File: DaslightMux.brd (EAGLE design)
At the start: 60 x 55.9 mm, 8 parts, among them U1 XC9572XL_TQ100

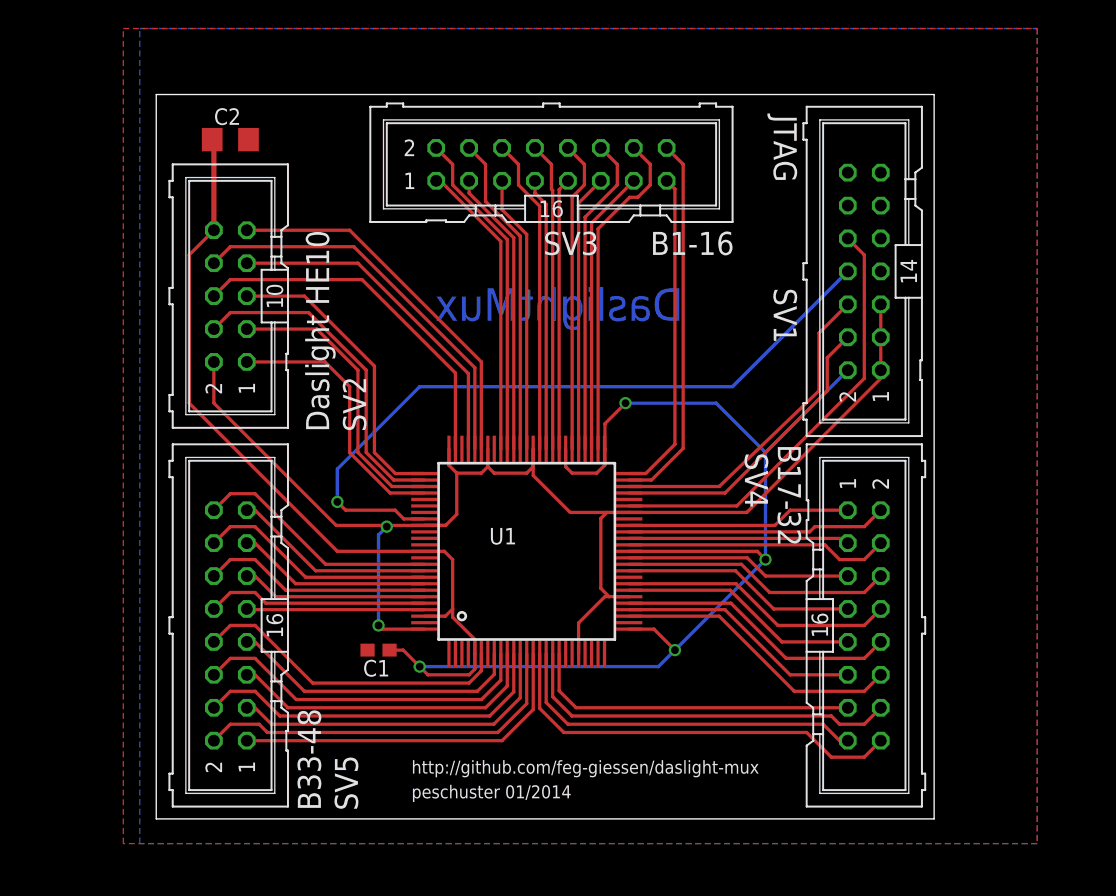
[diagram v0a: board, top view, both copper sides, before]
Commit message: Cleanup, enclosure.
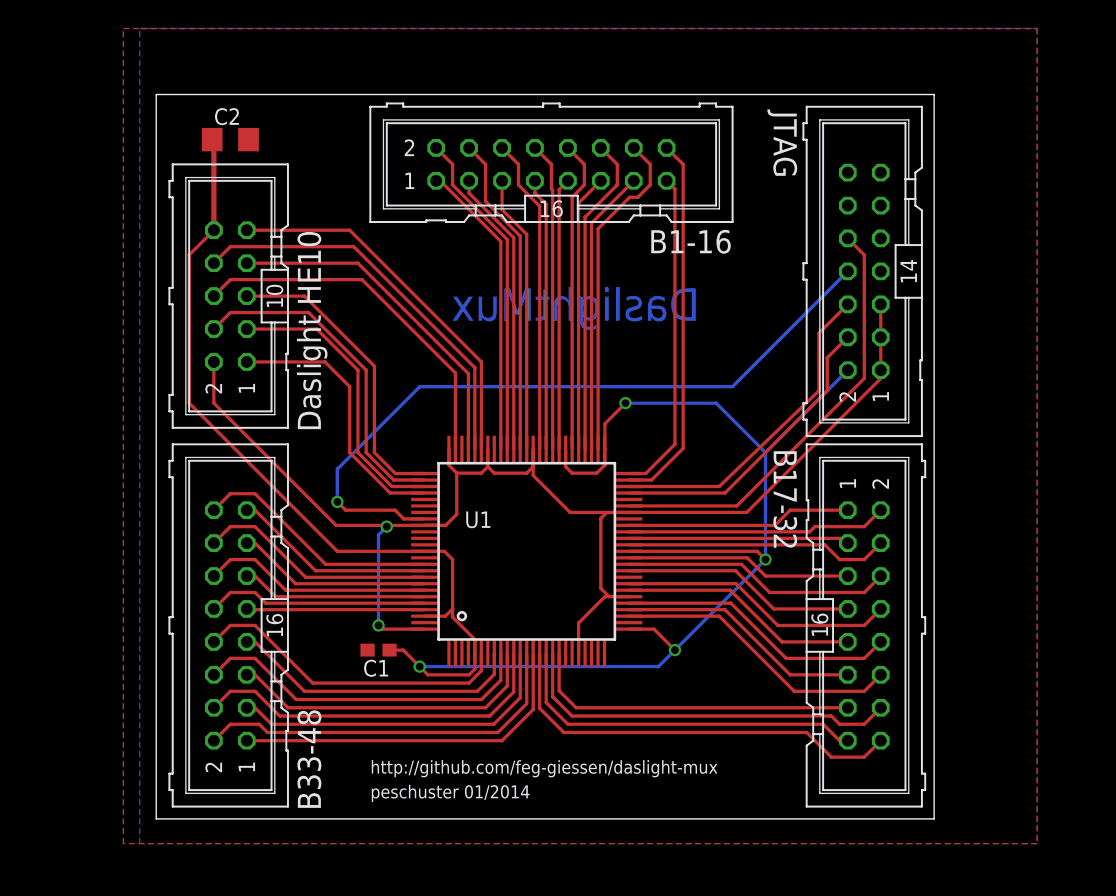
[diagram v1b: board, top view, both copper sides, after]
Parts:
- U1: value XC9572XL_TQ100 -> XC9572XL
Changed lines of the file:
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@@
 <wire x1="59.995" y1="55.87" x2="0" y2="55.87" width="0" layer="20"/>
 <wire x1="0" y1="55.87" x2="0" y2="0" width="0" layer="20"/>
-<text x="19.685" y="1.5875" size="1" layer="25">peschuster 01/2014</text>
-<text x="19.685" y="3.4925" size="1" layer="25">http://github.com/feg-giessen/daslight-mux</text>
-<text x="40.64" y="38.4175" size="2.5" layer="16" font="fixed" rot="MR0">DaslightMux</text>
+<text x="16.51" y="1.5875" size="1" layer="25">peschuster 01/2014</text>
+<text x="16.51" y="3.4925" size="1" layer="25">http://github.com/feg-giessen/daslight-mux</text>
+<text x="41.91" y="38.4175" size="2.5" layer="16" rot="MR0">DaslightMux</text>
 </plain>
 <attributes>
@@
 </autorouter>
 <elements>
-<element name="U1" library="xc9572xl-tq100" package="TQ100" value="XC9572XL_TQ100" x="28.575" y="20.6375"/>
+<element name="U1" library="xc9572xl-tq100" package="TQ100" value="XC9572XL" x="28.575" y="20.6375" smashed="yes">
+<attribute name="NAME" x="23.77" y="22.4425" size="1.27" layer="25"/>
+<attribute name="VALUE" x="23.77" y="20.1025" size="1.27" layer="27"/>
+</element>
 <element name="SV1" library="con-harting-ml" package="ML14" value="JTAG" x="54.61" y="42.2275" smashed="yes" rot="R90">
 <attribute name="OC_NEWARK" value="unknown" x="78.74" y="65.0875" size="1.778" layer="27" rot="R90" display="off"/>
@@
 <attribute name="MF" value="" x="78.74" y="65.0875" size="1.778" layer="27" rot="R90" display="off"/>
 <attribute name="OC_FARNELL" value="unknown" x="78.74" y="65.0875" size="1.778" layer="27" rot="R90" display="off"/>
-<attribute name="NAME" x="47.625" y="40.9575" size="1.778" layer="25" ratio="10" rot="SR270"/>
-<attribute name="VALUE" x="47.625" y="54.2925" size="1.778" layer="25" ratio="10" rot="SR270"/>
+<attribute name="VALUE" x="47.625" y="54.61" size="1.778" layer="25" ratio="10" rot="SR270"/>
 </element>
 <element name="SV2" library="con-harting-ml" package="ML10" value="Daslight HE10" x="5.715" y="40.3225" smashed="yes" rot="R90">
@@
 <attribute name="MF" value="" x="5.715" y="40.3225" size="1.778" layer="27" rot="R90" display="off"/>
 <attribute name="OC_FARNELL" value="unknown" x="5.715" y="40.3225" size="1.778" layer="27" rot="R90" display="off"/>
-<attribute name="NAME" x="16.1925" y="29.845" size="1.778" layer="25" ratio="10" rot="R90"/>
-<attribute name="VALUE" x="13.335" y="29.845" size="1.778" layer="25" ratio="10" rot="R90"/>
+<attribute name="VALUE" x="12.7" y="29.845" size="1.778" layer="25" ratio="10" rot="R90"/>
 </element>
 <element name="SV3" library="con-harting-ml" package="ML16" value="B1-16" x="30.48" y="50.4825" smashed="yes">
@@
 <attribute name="MF" value="" x="30.48" y="50.4825" size="1.778" layer="27" display="off"/>
 <attribute name="OC_FARNELL" value="unknown" x="30.48" y="50.4825" size="1.778" layer="27" display="off"/>
-<attribute name="NAME" x="29.845" y="43.4975" size="1.778" layer="25" ratio="10"/>
-<attribute name="VALUE" x="38.1" y="43.4975" size="1.778" layer="25" ratio="10"/>
+<attribute name="VALUE" x="44.45" y="45.4025" size="1.778" layer="25" ratio="10" rot="R180"/>
 </element>
 <element name="SV4" library="con-harting-ml" package="ML16" value="B17-32" x="54.61" y="14.9225" smashed="yes" rot="R270">
@@
 <attribute name="MF" value="" x="54.61" y="14.9225" size="1.778" layer="27" rot="R270" display="off"/>
 <attribute name="OC_FARNELL" value="unknown" x="54.61" y="14.9225" size="1.778" layer="27" rot="R270" display="off"/>
-<attribute name="NAME" x="45.4025" y="28.2575" size="1.778" layer="25" ratio="10" rot="SR270"/>
-<attribute name="VALUE" x="47.9425" y="28.8925" size="1.778" layer="25" ratio="10" rot="SR270"/>
+<attribute name="VALUE" x="47.625" y="28.575" size="1.778" layer="25" ratio="10" rot="SR270"/>
 </element>
 <element name="SV5" library="con-harting-ml" package="ML16" value="B33-48" x="5.715" y="14.9225" smashed="yes" rot="R90">
@@
 <attribute name="MF" value="" x="5.715" y="14.9225" size="1.778" layer="27" rot="R90" display="off"/>
 <attribute name="OC_FARNELL" value="unknown" x="5.715" y="14.9225" size="1.778" layer="27" rot="R90" display="off"/>
-<attribute name="NAME" x="15.5575" y="0.635" size="1.778" layer="25" ratio="10" rot="R90"/>
 <attribute name="VALUE" x="12.7" y="0.635" size="1.778" layer="25" ratio="10" rot="R90"/>
 </element>
-<element name="C1" library="resistor" package="C0603" value="100n" x="17.145" y="13.0175" rot="R180"/>
-<element name="C2" library="resistor" package="C1206" value="10u" x="5.715" y="52.3875"/>
+<element name="C1" library="resistor" package="C0603" value="100n" x="17.145" y="13.0175" smashed="yes" rot="R180">
+<attribute name="NAME" x="18.034" y="12.2555" size="1.27" layer="25" rot="R180"/>
+<attribute name="VALUE" x="18.034" y="10.6045" size="1.27" layer="27" rot="R180"/>
+</element>
+<element name="C2" library="resistor" package="C1206" value="10u" x="5.715" y="52.3875" smashed="yes">
+<attribute name="NAME" x="4.445" y="53.5305" size="1.27" layer="25"/>
+<attribute name="VALUE" x="7.9375" y="53.467" size="1.27" layer="27"/>
+</element>
 </elements>
 <signals>

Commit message: Schematic & enclosure
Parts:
- added EXT_VCC, GND: LSP10, solpad:LSP10
- added SJ1: (no value), jumper:SJ_2
- SV2: value Daslight HE10 -> HE10
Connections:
- new net N$1: SJ1.1, SV2.10
- new net N$2: EXT_VCC.MP, SJ1.3
- net GND: now also GND.MP
- net VCC: now also SJ1.2; no longer SV2.10
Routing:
- net VCC: track 150.6 -> 161.5 mm
- net N$1: track 0.00 -> 9.44 mm
- net N$2: track 0.00 -> 3.56 mm
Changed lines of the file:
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@@
 <setting verticaltext="up"/>
 </settings>
-<grid distance="25" unitdist="mil" unit="mm" style="lines" multiple="1" display="no" altdistance="0.0125" altunitdist="inch" altunit="mil"/>
+<grid distance="25" unitdist="mil" unit="mil" style="lines" multiple="1" display="no" altdistance="0.0125" altunitdist="inch" altunit="mil"/>
 <layers>
 <layer number="1" name="Top" color="4" fill="1" visible="yes" active="yes"/>
@@
 <layer number="43" name="vRestrict" color="2" fill="10" visible="yes" active="yes"/>
 <layer number="44" name="Drills" color="7" fill="1" visible="no" active="yes"/>
-<layer number="45" name="Holes" color="7" fill="1" visible="no" active="yes"/>
+<layer number="45" name="Holes" color="7" fill="1" visible="yes" active="yes"/>
 <layer number="46" name="Milling" color="3" fill="1" visible="no" active="yes"/>
 <layer number="47" name="Measures" color="7" fill="1" visible="no" active="yes"/>
@@
 <wire x1="59.995" y1="55.87" x2="0" y2="55.87" width="0" layer="20"/>
 <wire x1="0" y1="55.87" x2="0" y2="0" width="0" layer="20"/>
-<text x="16.51" y="1.5875" size="1" layer="25">peschuster 01/2014</text>
-<text x="16.51" y="3.4925" size="1" layer="25">http://github.com/feg-giessen/daslight-mux</text>
-<text x="41.91" y="38.4175" size="2.5" layer="16" rot="MR0">DaslightMux</text>
+<text x="15.24" y="6.0325" size="1" layer="25">peschuster 01/2014</text>
+<text x="15.24" y="7.9375" size="1" layer="25">http://github.com/feg-giessen/daslight-mux</text>
+<text x="41.91" y="40.3225" size="2.5" layer="16" font="vector" rot="MR0">DaslightMux</text>
+<hole x="18" y="3.5" drill="3.2"/>
+<hole x="42" y="3.5" drill="3.2"/>
+<hole x="37" y="35" drill="3.2"/>
 </plain>
 <attributes>
@@
 <element name="U1" library="xc9572xl-tq100" package="TQ100" value="XC9572XL" x="28.575" y="20.6375" smashed="yes">
 <attribute name="NAME" x="23.77" y="22.4425" size="1.27" layer="25"/>
-<attribute name="VALUE" x="23.77" y="20.1025" size="1.27" layer="27"/>
+<attribute name="VALUE" x="23.77" y="20.1025" size="1.27" layer="25"/>
 </element>
 <element name="SV1" library="con-harting-ml" package="ML14" value="JTAG" x="54.61" y="42.2275" smashed="yes" rot="R90">
@@
 <attribute name="MF" value="" x="78.74" y="65.0875" size="1.778" layer="27" rot="R90" display="off"/>
 <attribute name="OC_FARNELL" value="unknown" x="78.74" y="65.0875" size="1.778" layer="27" rot="R90" display="off"/>
-<attribute name="VALUE" x="47.625" y="54.61" size="1.778" layer="25" ratio="10" rot="SR270"/>
+<attribute name="VALUE" x="47.625" y="41.275" size="1.778" layer="25" ratio="10" rot="SR270"/>
 </element>
-<element name="SV2" library="con-harting-ml" package="ML10" value="Daslight HE10" x="5.715" y="40.3225" smashed="yes" rot="R90">
+<element name="SV2" library="con-harting-ml" package="ML10" value="HE10" x="5.715" y="40.3225" smashed="yes" rot="R90">
 <attribute name="OC_NEWARK" value="unknown" x="5.715" y="40.3225" size="1.778" layer="27" rot="R90" display="off"/>
 <attribute name="MPN" value="" x="5.715" y="40.3225" size="1.778" layer="27" rot="R90" display="off"/>
@@
 <element name="C1" library="resistor" package="C0603" value="100n" x="17.145" y="13.0175" smashed="yes" rot="R180">
 <attribute name="NAME" x="18.034" y="12.2555" size="1.27" layer="25" rot="R180"/>
-<attribute name="VALUE" x="18.034" y="10.6045" size="1.27" layer="27" rot="R180"/>
+<attribute name="VALUE" x="15.1765" y="12.192" size="1.27" layer="27" rot="R180"/>
 </element>
 <element name="C2" library="resistor" package="C1206" value="10u" x="5.715" y="52.3875" smashed="yes">
@@
 <attribute name="VALUE" x="7.9375" y="53.467" size="1.27" layer="27"/>
 </element>
+<element name="SJ1" library="jumper" package="SJ_2" value="" x="13.335" y="48.26" rot="R90"/>
+<element name="EXT_VCC" library="solpad" package="LSP10" value="LSP10" x="13.335" y="53.34" smashed="yes">
+<attribute name="NAME" x="16.1925" y="46.355" size="1.27" layer="25" ratio="10" rot="R90"/>
+<attribute name="VALUE" x="13.335" y="53.594" size="0.0254" layer="27"/>
+</element>
+<element name="GND" library="solpad" package="LSP10" value="LSP10" x="47.625" y="52.07" rot="R90"/>
 </elements>
 <signals>
@@
 <contactref element="C1" pad="2"/>
 <contactref element="C2" pad="2"/>
+<contactref element="GND" pad="MP"/>
 </signal>
 <signal name="TMS">
@@
 <contactref element="SV1" pad="8"/>
 <contactref element="U1" pad="83"/>
-<wire x1="53.34" y1="42.2275" x2="44.45" y2="33.3375" width="0.254" layer="16"/>
-<wire x1="44.45" y1="33.3375" x2="20.32" y2="33.3375" width="0.254" layer="16"/>
-<wire x1="20.32" y1="33.3375" x2="13.97" y2="26.9875" width="0.254" layer="16"/>
+<wire x1="53.34" y1="42.2275" x2="43.815" y2="32.7025" width="0.254" layer="16"/>
+<wire x1="43.815" y1="32.7025" x2="19.685" y2="32.7025" width="0.254" layer="16"/>
+<wire x1="19.685" y1="32.7025" x2="13.97" y2="26.9875" width="0.254" layer="16"/>
 <wire x1="13.97" y1="26.9875" x2="13.97" y2="24.4475" width="0.254" layer="16"/>
 <wire x1="20.675" y1="23.1375" x2="19.09" y2="23.1375" width="0.254" layer="1"/>
@@
 <wire x1="34.6075" y1="27.305" x2="34.6075" y2="28.505" width="0.254" layer="1"/>
 <wire x1="34.6075" y1="28.505" x2="34.575" y2="28.5375" width="0.254" layer="1"/>
-<contactref element="SV2" pad="10"/>
 <contactref element="U1" pad="98"/>
 <wire x1="20.675" y1="20.6375" x2="22.225" y2="20.6375" width="0.254" layer="1"/>
@@
 <wire x1="20.675" y1="20.6375" x2="13.97" y2="20.6375" width="0.254" layer="1"/>
 <wire x1="13.97" y1="20.6375" x2="2.54" y2="32.0675" width="0.254" layer="1"/>
-<wire x1="2.54" y1="32.0675" x2="2.54" y2="43.4975" width="0.254" layer="1"/>
-<wire x1="2.54" y1="43.4975" x2="4.445" y2="45.4025" width="0.254" layer="1"/>
+<wire x1="2.54" y1="32.0675" x2="2.54" y2="50.6125" width="0.254" layer="1"/>
 <wire x1="36.475" y1="20.6375" x2="46.355" y2="20.6375" width="0.254" layer="1"/>
 <wire x1="46.355" y1="20.6375" x2="46.99" y2="20.0025" width="0.254" layer="1"/>
@@
 <wire x1="46.99" y1="28.2575" x2="46.99" y2="20.0025" width="0.254" layer="16"/>
 <wire x1="33.9725" y1="26.67" x2="34.6075" y2="27.305" width="0.254" layer="1"/>
-<wire x1="34.6075" y1="28.505" x2="34.6075" y2="30.48" width="0.254" layer="1"/>
-<wire x1="34.6075" y1="30.48" x2="36.195" y2="32.0675" width="0.254" layer="1"/>
-<via x="36.195" y="32.0675" extent="1-16" drill="0.6" shape="octagon"/>
-<wire x1="36.195" y1="32.0675" x2="43.18" y2="32.0675" width="0.254" layer="16"/>
-<wire x1="43.18" y1="32.0675" x2="46.99" y2="28.2575" width="0.254" layer="16"/>
+<wire x1="34.6075" y1="28.505" x2="34.6075" y2="29.845" width="0.254" layer="1"/>
+<wire x1="34.6075" y1="29.845" x2="36.195" y2="31.4325" width="0.254" layer="1"/>
+<via x="36.195" y="31.4325" extent="1-16" drill="0.6" shape="octagon"/>
+<wire x1="36.195" y1="31.4325" x2="43.815" y2="31.4325" width="0.254" layer="16"/>
+<wire x1="43.815" y1="31.4325" x2="46.99" y2="28.2575" width="0.254" layer="16"/>
 <wire x1="24.575" y1="12.7375" x2="24.575" y2="11.5575" width="0.254" layer="1"/>
 <wire x1="24.575" y1="11.5575" x2="24.13" y2="11.1125" width="0.254" layer="1"/>
@@
 <wire x1="17.995" y1="13.0175" x2="19.05" y2="13.0175" width="0.254" layer="1"/>
 <wire x1="19.05" y1="13.0175" x2="20.32" y2="11.7475" width="0.254" layer="1"/>
-<wire x1="4.445" y1="45.4025" x2="4.445" y2="52.2575" width="0.4064" layer="1"/>
 <wire x1="4.445" y1="52.2575" x2="4.315" y2="52.3875" width="0.4064" layer="1"/>
+<contactref element="SJ1" pad="2"/>
+<wire x1="2.54" y1="50.6125" x2="3.90375" y2="51.97625" width="0.254" layer="1"/>
+<wire x1="3.90375" y1="51.97625" x2="4.315" y2="52.3875" width="0.254" layer="1"/>
+<wire x1="13.335" y1="48.26" x2="6.35" y2="48.26" width="0.6096" layer="1"/>
+<wire x1="6.35" y1="48.26" x2="4.445" y2="50.165" width="0.6096" layer="1"/>
+<wire x1="4.445" y1="50.165" x2="4.445" y2="51.435" width="0.6096" layer="1"/>
+<wire x1="4.445" y1="51.435" x2="3.90375" y2="51.97625" width="0.254" layer="1"/>
 </signal>
 <signal name="B40">
@@
 <wire x1="22.86" y1="50.4825" x2="21.59" y2="51.7525" width="0.254" layer="1"/>
 </signal>
+<signal name="N$1">
+<contactref element="SV2" pad="10"/>
+<contactref element="SJ1" pad="1"/>
+<wire x1="13.335" y1="46.736" x2="5.7785" y2="46.736" width="0.6096" layer="1"/>
+<wire x1="5.7785" y1="46.736" x2="4.445" y2="45.4025" width="0.6096" layer="1"/>
+</signal>
+<signal name="N$2">
+<contactref element="SJ1" pad="3"/>
+<contactref element="EXT_VCC" pad="MP"/>
+<wire x1="13.335" y1="53.34" x2="13.335" y2="49.784" width="0.8128" layer="1"/>
+</signal>
 </signals>
